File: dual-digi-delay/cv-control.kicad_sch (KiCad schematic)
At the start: 55 parts, among them Q1 2N3904, Q2 2N3904, Q3 2N3904, Q4 2N3904, U4 TL074, U5 TL074

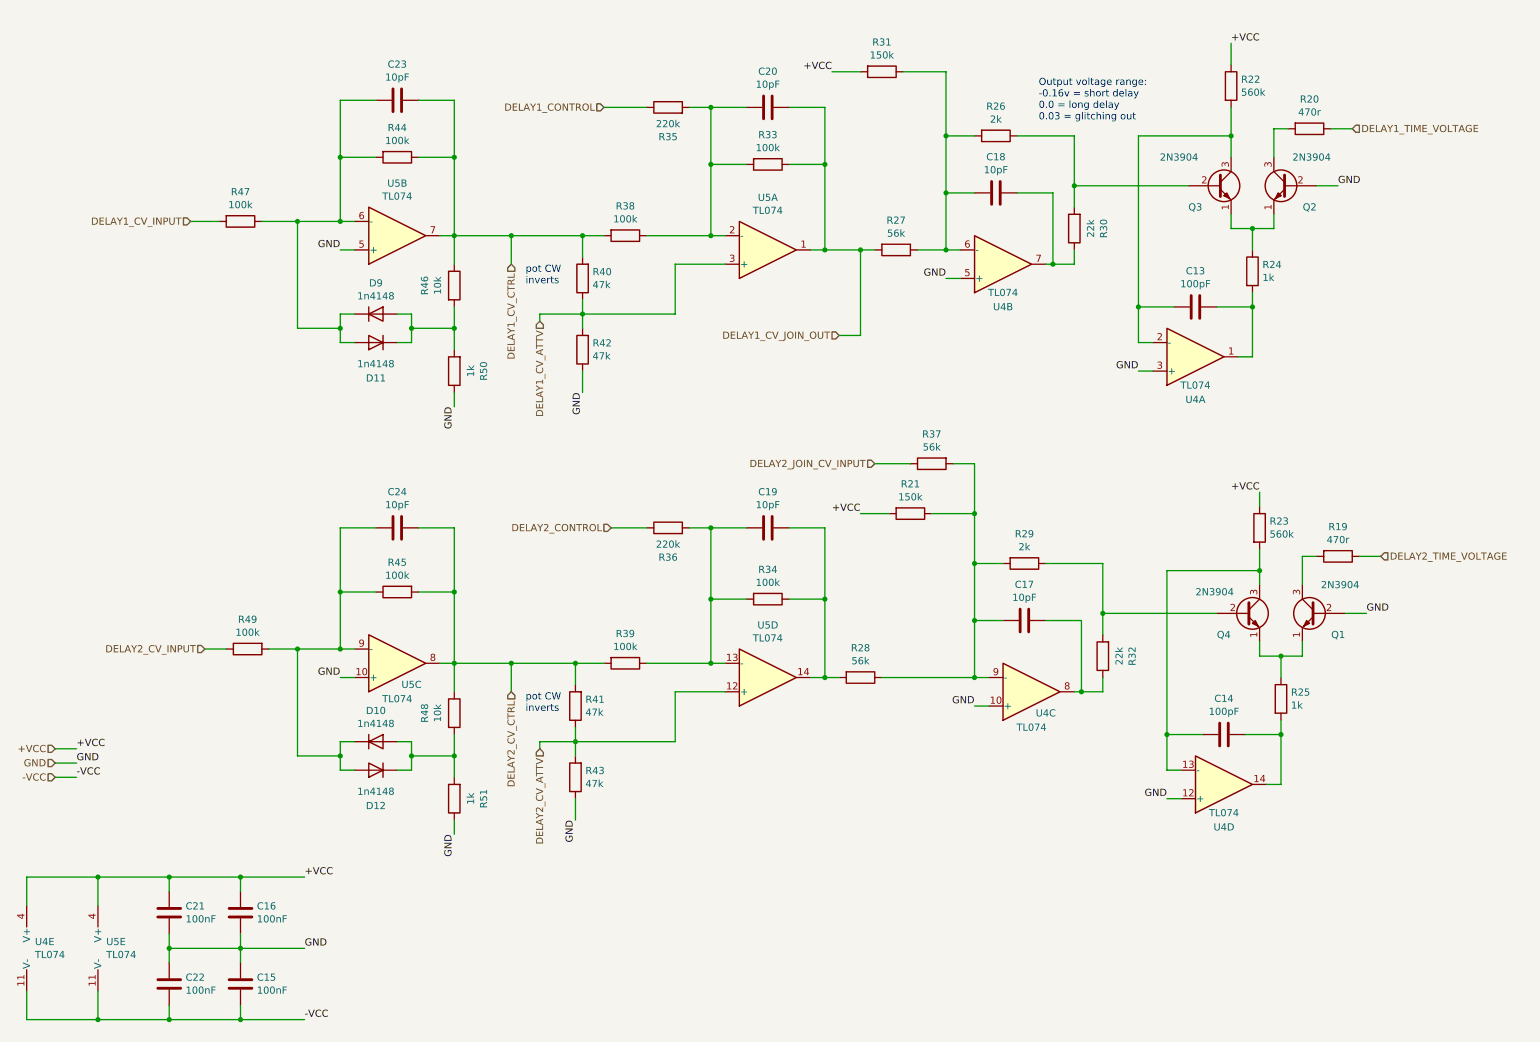
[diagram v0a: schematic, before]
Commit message: Making temporary branch for rev2 builds
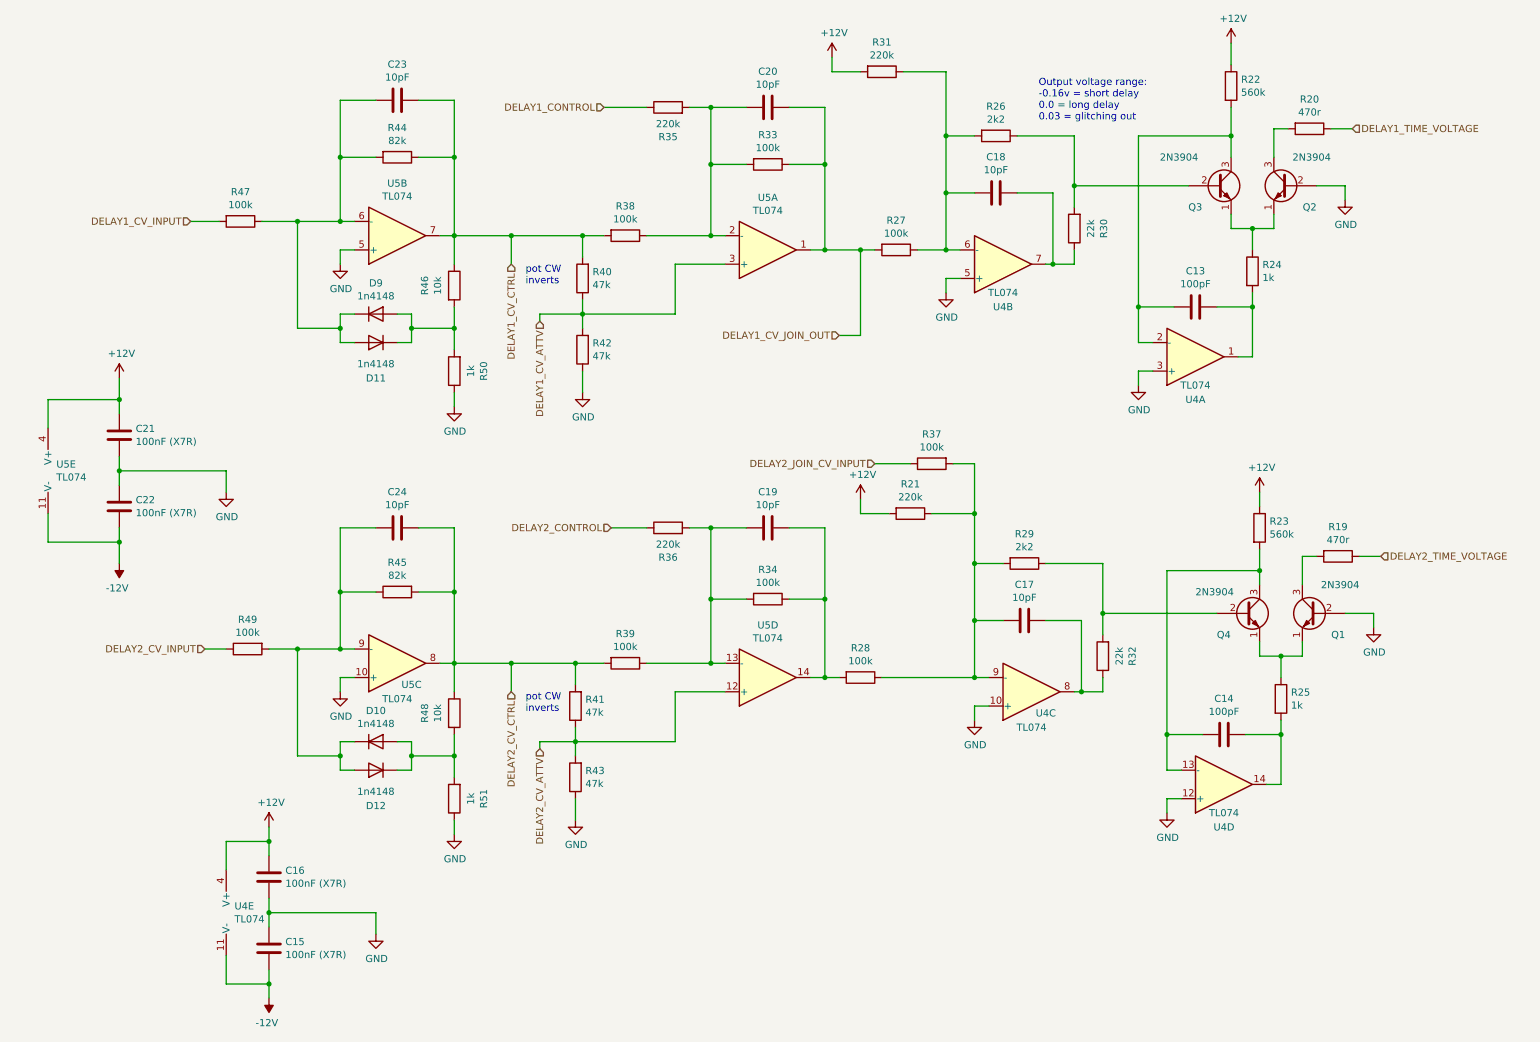
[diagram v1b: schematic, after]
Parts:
- C15, C16, C21, C22: value 100nF -> 100nF (X7R)
- R21, R31: value 150k -> 220k
- R26, R29: value 2k -> 2k2
- R27, R28, R37: value 56k -> 100k
- R44, R45: value 100k -> 82k
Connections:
- net +VCC renamed +12V
- net -VCC renamed -12V
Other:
- moved on the sheet: C15, C16, C21, C22, U4E, U5E
